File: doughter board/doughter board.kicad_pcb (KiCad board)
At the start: 2 copper layers, 52.7 x 25.4 mm, 39 parts, among them J1 BOOT_TO/ SELECTOR, J2 BOOT_TO/ SELECTOR, J3 Conn_01x05, J4 RS 485, J5 UART2, J6 OUTPUT, J7 Serial_BUS, SW1 SW_SPST, U1 LM1117-3.3, U2 SN65HVD11, U3 STM32F030C6Tx, Y1 8 MHz

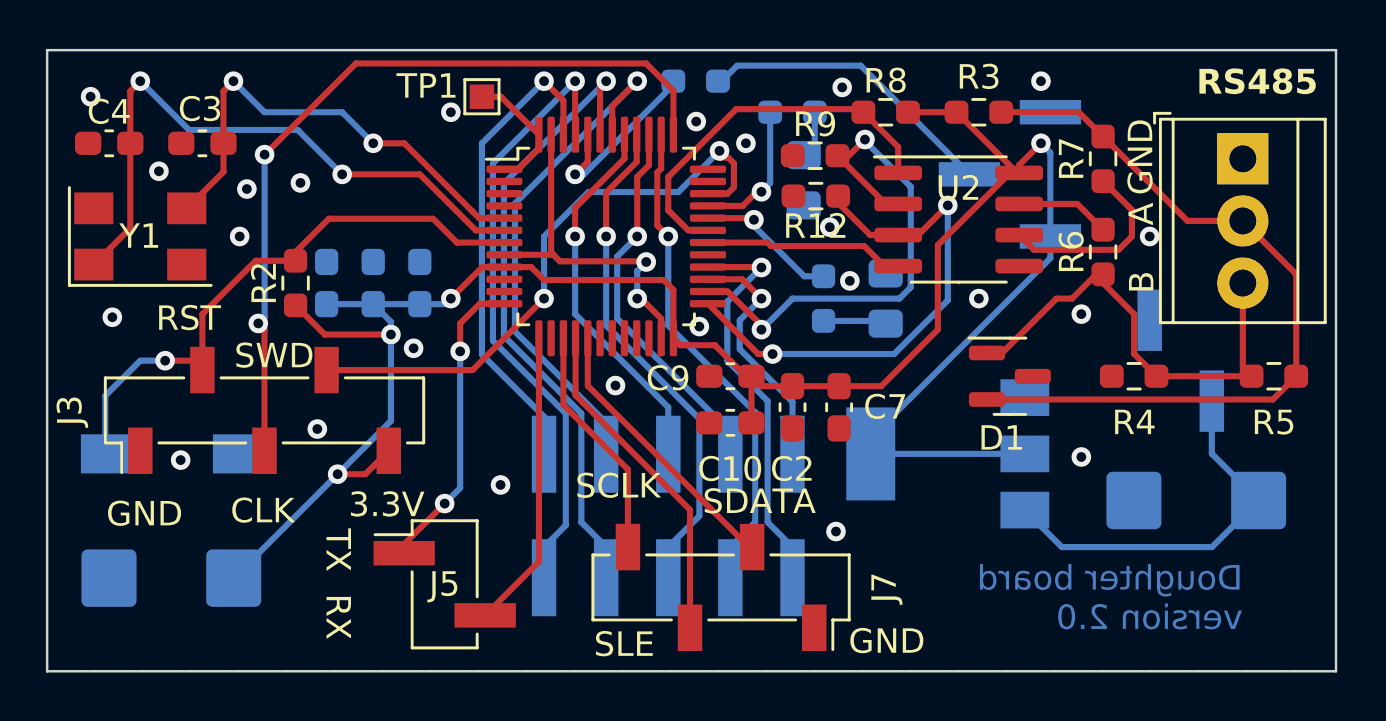
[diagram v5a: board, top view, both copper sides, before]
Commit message: Minor fixes for doughterboard and added backup zips for mother
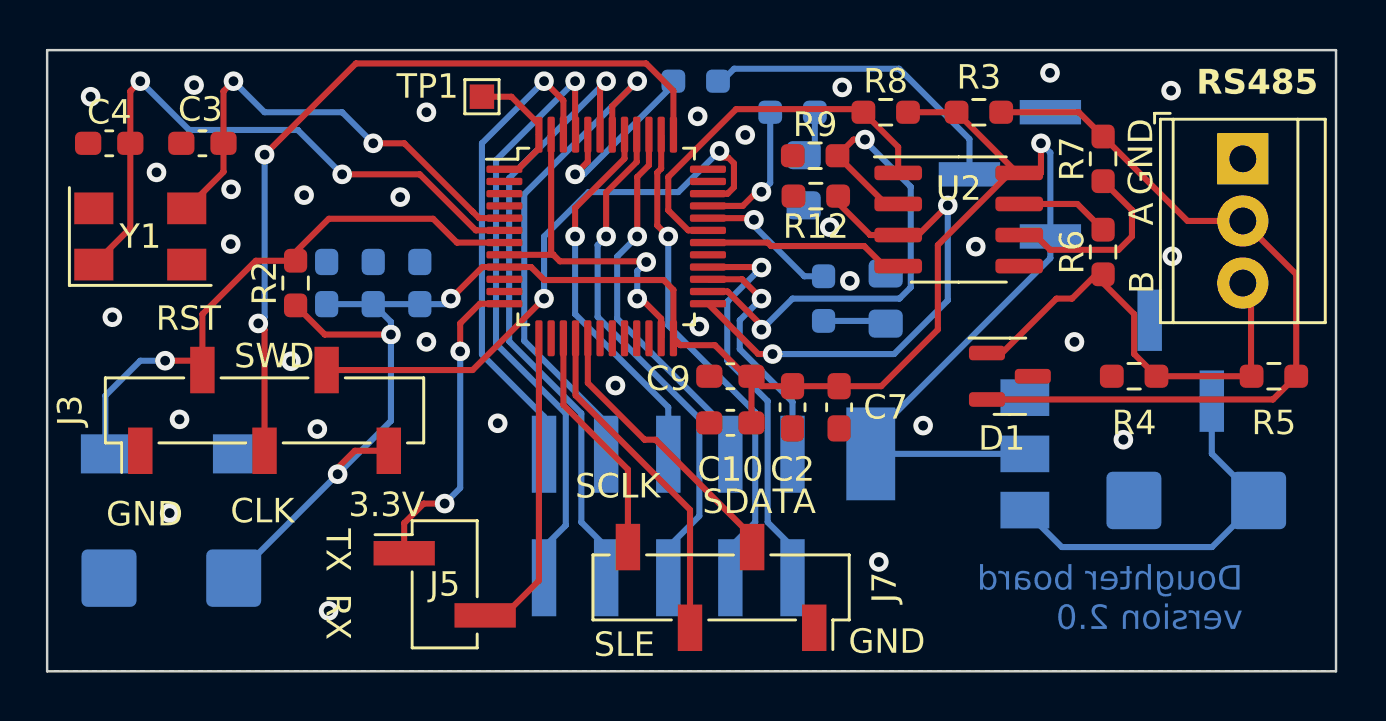
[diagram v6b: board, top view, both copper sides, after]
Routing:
- net Net-(J1-Pin_2): track 12.2 -> 13.0 mm
- net VDD: track 90.1 -> 90.7 mm
- net /UART2_TX: track 12.5 -> 13.0 mm
- net GND: vias 24 -> 31
